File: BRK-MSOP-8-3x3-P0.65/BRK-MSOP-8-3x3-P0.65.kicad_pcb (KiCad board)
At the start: 2 copper layers, 18.3 x 22.6 mm, 3 parts, among them J1 Conn_01x04, J2 Conn_01x04, U1 MSOP-8-3x3-P0.65

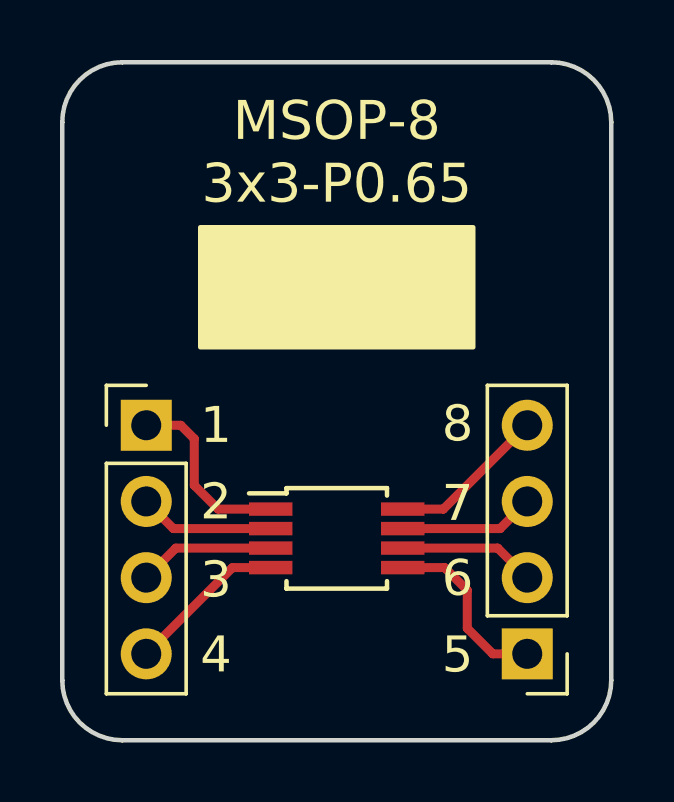
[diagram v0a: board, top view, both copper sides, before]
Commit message: Update several breakout boards
* Reduce distance from edge to pin header
* Enlarge silk screen area
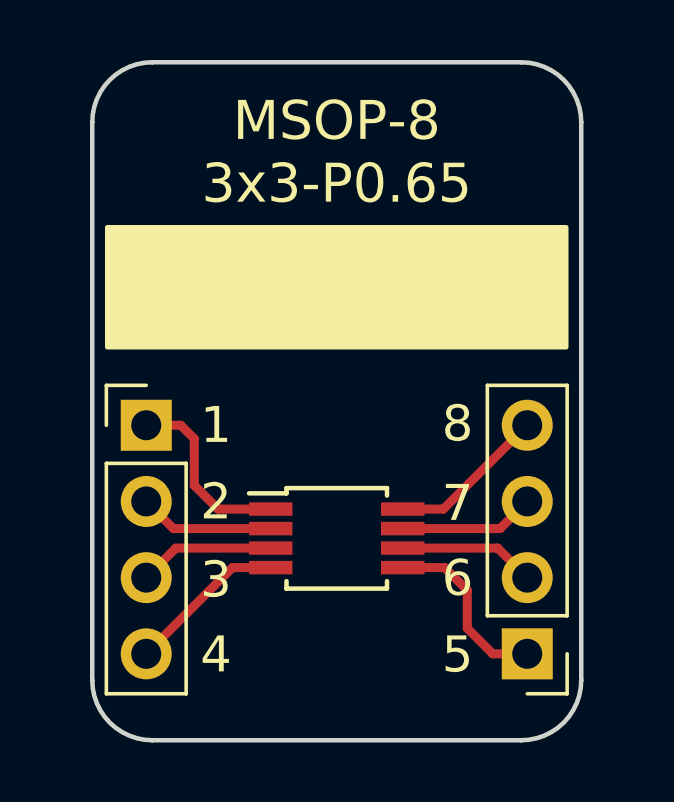
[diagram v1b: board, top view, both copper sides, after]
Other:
- board size 18.3 x 22.6 mm -> 16.3 x 22.6 mm
